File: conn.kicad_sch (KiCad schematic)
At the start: 39 parts, among them J401 PWR IN, J402 Toolhead 1, J403 Toolhead 2, J404 XH, J405 IN, J406 OUT, J407 OUT, Q401 CJAC70P06, U401 TJA1051TK-3, U402 CH334F, U403 USBLC6-2SC6, U404 USBLC6-2SC6, U405 USBLC6-2SC6

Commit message: Major hardware update: toolhead switching, DC/DC protection, and documentation overhaul
Hardware Changes:
- Replaced reverse polarity protection with 2x PFET toolhead switching (PB2/PA5 control)
- Added SS56 Schottky diode reverse polarity protection for DC/DC converter
- Updated current limit resistor to 5.1kΩ (~10.2A)
- Removed fan control circuitry and JST-XH connector
- Removed internal JST-XH USB port with fuse/protection

Documentation Updates:
- Updated both README files to reflect hardware changes
- Removed all fan control references and configurations
- Updated Klipper configuration examples
- Cleaned up pinout and connector assignments
- Updated technical specifications table
- Fixed table of contents and cross-references
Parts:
- removed F405: 1.5A, Fuse:Fuse_0805_2012Metric, symbol Device:Fuse_Small
- removed J404: XH, Connector_JST:JST_XH_B4B-XH-A_1x04_P2.50mm_Vertical, symbol Connector:Conn_01x04_Pin
- removed R402: 30k, Resistor_SMD:R_0402_1005Metric, symbol Device:R
- added D402: D_Schottky, Diode_SMD:D_SMC, symbol Device:D_Schottky
- added D407: BZT52C15S, Diode_SMD:D_SOD-323, symbol Device:D_Zener_Small
- added Q403, Q405: AO3400A, Package_TO_SOT_SMD:SOT-23, symbol Transistor_FET:AO3400A
- added Q404: CJAC70P06, Package_DFN_QFN:AO_DFN-8-1EP_5.55x5.2mm_P1.27mm_EP4.12x4.6mm, symbol Transistor_FET:AON6411
- added R403, R406, R413, R414, R415: 30k, Resistor_SMD:R_0402_1005Metric, symbol Device:R
- added R407, R416: 1k, Resistor_SMD:R_0402_1005Metric, symbol Device:R
- renumbered D402 to D404, D404 to D406, R403 to R405, R404 to R408, R405 to R409, R406 to R410, R407 to R411, R408 to R412
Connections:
- net 24V: now also D402.1 (K); no longer F401.1, F402.1, Q401.5 (D)
- net GND: now also Q403.2 (S), Q405.2 (S), R406.1, R415.1
- net OUT1: now also F401.1, Q404.5 (D); no longer F401.2, J402.1 (Pin_1)
- net OUT2: now also F402.1, Q401.5 (D); no longer F402.2, J403.1 (Pin_1)
- net VEXT: now also D402.2 (A), D407.1 (K), Q404.1 (S), Q404.2 (S), Q404.3 (S), R413.1
- net GATE renamed HE GATE 2
- net HE GATE 2: now also R403.1
- new net: Q405.1 (G), R415.2, R416.1
- new net: Q403.1 (G), R406.2, R407.1
- new net: Q403.3 (D), R403.2
- new net: Q405.3 (D), R414.2
- new net HE GATE 1: D407.2 (A), Q404.4 (G), R413.2, R414.1
- new net HE1 ON: R416.2
- new net HE2 ON: R407.2
- new net OUT1F: F401.2, J402.1 (Pin_1)
- new net OUT2F: F402.2, J403.1 (Pin_1)
- no-connect marks 4 -> 12
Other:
- company: (none) -> Eduard Iten
- title: (none) -> EWS - Power, CANbus and USB HAT for 3D Printers
- moved on the sheet: C401, C402, C403, C404, D403, D404, D405, D406, F401, F402, F404, J402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

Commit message: EWS Rev 0.1 - Complete design with documentation
Release Features:
- Universal HAT for Raspberry Pi 4/5 and Radxa Rock 5B/5B+
- 8A DC/DC converter with SS56 reverse polarity protection
- Dual toolhead switching via PFETs (PB2/PA5 control)
- Native CAN and USB-CAN bridge support
- USB hub with power delivery for touchscreens
- Comprehensive safety features and thermal management

Hardware:
- STM32G0B1KBU6 MCU with crystal-less design
- MaxLinear XR76208 switching regulator
- MCP2542WFD CAN transceiver with jumper selection
- WCH CH334F USB hub with MTT support
- 2oz copper PCB recommended for thermal performance

Documentation:
- Bilingual documentation (German/English)
- Installation guides with kernel diagnostics
- Klipper configuration examples
- Comprehensive problem statement and solutions
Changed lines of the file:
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@@
 	)
 	(junction
-		(at 186.69 78.74)
-		(diameter 0)
-		(color 0 0 0 0)
-	)
-	(junction
 		(at 246.38 45.72)
 		(diameter 0)
@@
 	)
 	(junction
-		(at 186.69 33.02)
-		(diameter 0)
-		(color 0 0 0 0)
-	)
-	(junction
 		(at 88.9 189.23)
 		(diameter 0)
@@
 	)
 	(junction
+		(at 186.69 78.74)
+		(diameter 0)
+		(color 0 0 0 0)
+	)
+	(junction
 		(at 163.83 99.06)
 		(diameter 0)
@@
 	(wire
 		(pts
+			(xy 186.69 76.2) (xy 186.69 78.74)
+		)
+		(stroke
+			(width 0)
+			(type default)
+		)
+	)
+	(wire
+		(pts
 			(xy 60.96 148.59) (xy 60.96 153.67)
 		)
@@
 	(wire
 		(pts
-			(xy 186.69 33.02) (xy 186.69 78.74)
-		)
-		(stroke
-			(width 0)
-			(type default)
-		)
-	)
-	(wire
-		(pts
 			(xy 266.7 157.48) (xy 266.7 158.75)
 		)
@@
 					(unit 1)
 				)
+			)
+		)
+	)
+	(symbol
+		(lib_id "power:+5V")
+		(at 186.69 76.2 0)
+		(unit 1)
+		(exclude_from_sim no)
+		(in_bom yes)
+		(on_board yes)
+		(dnp no)
+		(fields_autoplaced yes)
+		(property "Reference" "#PWR0411"
+			(at 186.69 80.01 0)
+			(effects
+				(font
+					(size 1.27 1.27)
+				)
+				(hide yes)
+			)
+		)
+		(property "Value" "5V"
+			(at 186.69 71.12 0)
+			(effects
+				(font
+					(size 1.27 1.27)
+				)
+			)
+		)
+		(property "Footprint" ""
+			(at 186.69 76.2 0)
+			(effects
+				(font
+					(size 1.27 1.27)
+				)
+				(hide yes)
+			)
+		)
+		(property "Datasheet" ""
+			(at 186.69 76.2 0)
+			(effects
+				(font
+					(size 1.27 1.27)
+				)
+				(hide yes)
+			)
+		)
+		(property "Description" "Power symbol creates a global label with name \"+5V\""
+			(at 186.69 76.2 0)
+			(effects
+				(font
+					(size 1.27 1.27)
+				)
+				(hide yes)
+			)
+		)
+		(pin "1"
+		)
+		(instances
+			(project "EWS"
+				(path "/4ae99543-64c8-472f-befd-04c32f138656/7e492d82-58e4-4d5e-a79a-918a5cf15050"
+					(reference "#PWR0411")
+					(unit 1)
+				)

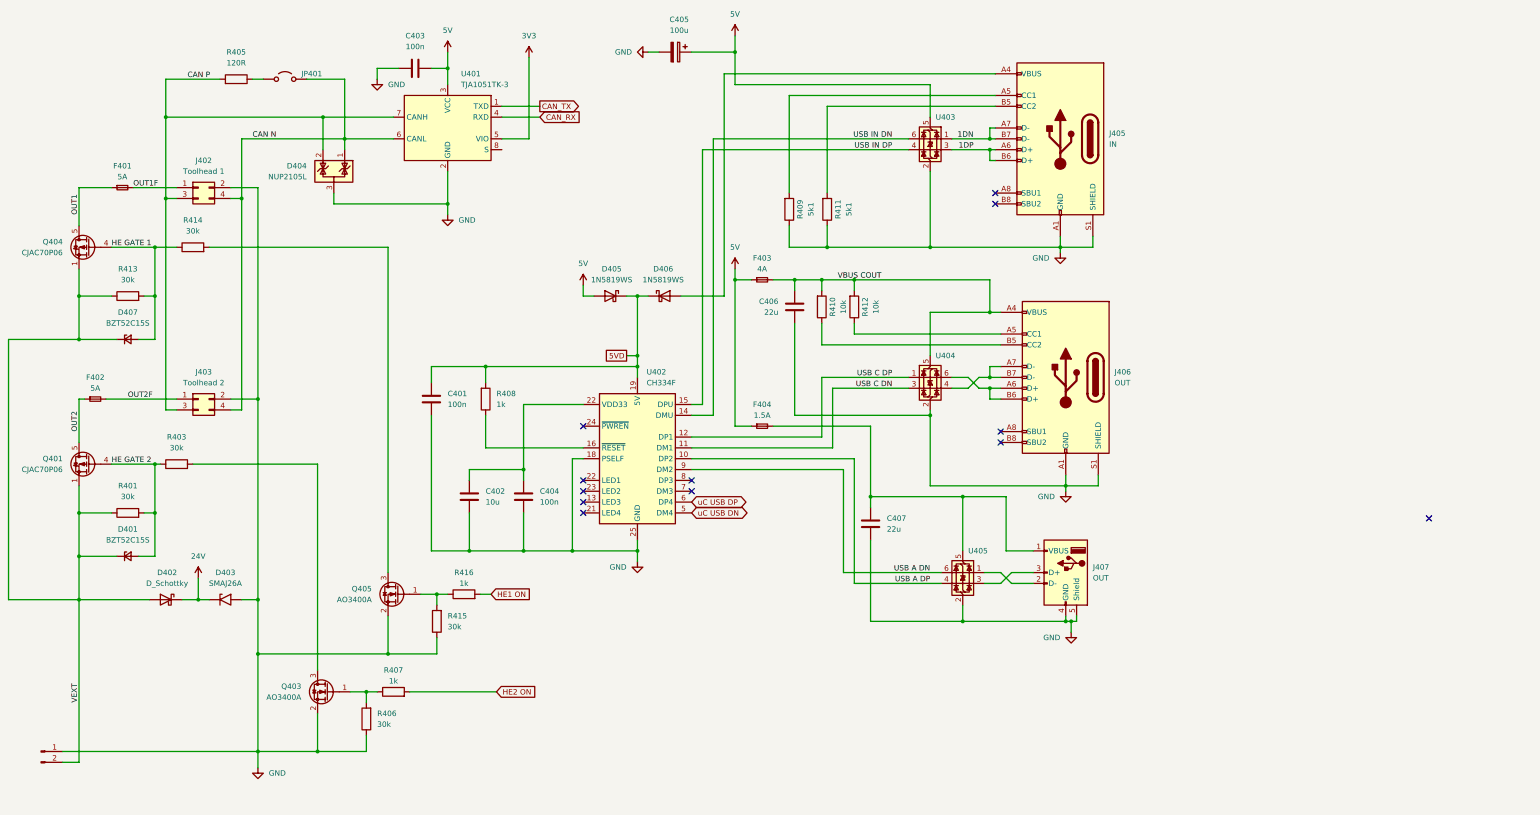
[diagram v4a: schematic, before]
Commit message: Schema improvements and CAN transceiver modification
- Improved schema layout for better readability and organization
- Connected CAN transceiver S-pin to GND for proper operation
- Updated PCB layout to reflect schema changes
- Enhanced component placement and routing clarity
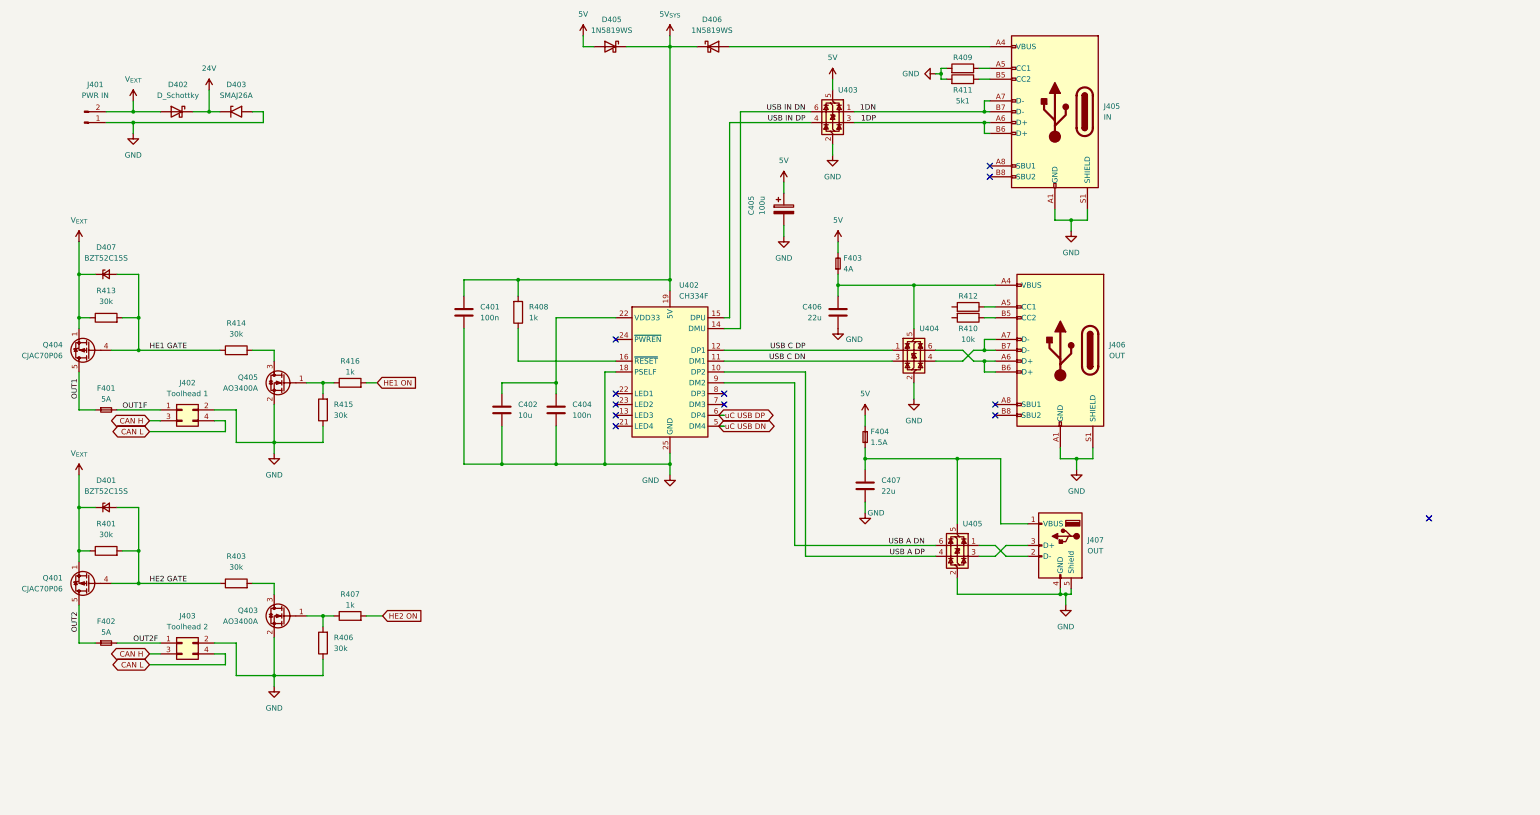
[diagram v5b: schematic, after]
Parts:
- removed C403: 100n, Capacitor_SMD:C_0402_1005Metric, symbol Device:C
- removed D404: NUP2105L, Package_TO_SOT_SMD:SOT-23, symbol Power_Protection:NUP2105L
- removed JP401: ~, Connector_PinHeader_2.54mm:PinHeader_1x02_P2.54mm_Vertical, symbol Jumper:Jumper_2_Open
- removed R405: 120R, Resistor_SMD:R_0402_1005Metric_Pad0.72x0.64mm_HandSolder, symbol Device:R
- removed U401: TJA1051TK-3, Package_SON:HVSON-8-1EP_3x3mm_P0.65mm_EP1.6x2.4mm, symbol Interface_CAN_LIN:TJA1051TK-3
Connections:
- net 5V: now also F403.2; no longer F403.1
- net GND: now also R409.2, R411.2; no longer R409.1, R411.1
- net at J405.B5 (CC2): now also R411.1; no longer R411.2
- net at J405.A5 (CC1): now also R409.1; no longer R409.2
- net 5VD renamed 5V_{SYS}
- net CAN N renamed CAN L
- net CAN P renamed CAN H
- net HE GATE 1 renamed HE1 GATE
- net HE GATE 2 renamed HE2 GATE
- net VBUS COUT: no longer names the net of C406.1, J406.A4 (VBUS), J406.A9 (VBUS), J406.B4 (VBUS), J406.B9 (VBUS), U404.5 (VBUS)
- net VBUS COUT: now also F403.1; no longer F403.2, R410.2, R412.2
- net VEXT renamed V_{EXT}
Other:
- moved on the sheet: C401, C402, C404, C405, C406, C407, D401, D402, D403, D405, D406, D407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

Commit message: Rev 0.2: Major hardware improvements and production readiness
Hardware Improvements (Thanks to shx for schematic cleanup):
- Clean up schematic organization and structure
- Set CAN transceiver Silent pin to GND for stability
- Add status LEDs (yellow: 24V/5V/3.3V, green: MCU PB4)
- Replace jumpers with solder jumpers on bottom side
- Add jumpers to output PFETs for permanent-on without firmware
- Add robust test points for 5V/GND load testing
- Add optional heatsink for DC/DC converter on bottom
- Add 10µF capacitor for MCU on 3.3V rail

Component Optimizations:
- Replace 30kΩ with 33kΩ basic part for simplified BOM
- Change DC/DC feedback: 15.5kΩ15kΩ (new output: 5.1V)
- Upgrade CAN ESD protection: NUP2105LPESD1CAN
- Increase CAN termination resistor footprint: 04020603
- Switch USB hub supply from 5V to 3.3V per datasheet

Production Ready:
- Add all LCSC part numbers and rotations
- Generate complete production data package
- Improve PCB layout and button placement
- Create comprehensive changelog documentation
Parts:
- removed R416: 1k, Resistor_SMD:R_0402_1005Metric, symbol Device:R
- added JP401, JP402: ~, project:SolderJumper-3_P1.3mm_Bridged12_RoundedPad1.0x1.5mm_custom, symbol Jumper:Jumper_3_Bridged12
- C401, C404: LCSC Part # (none) -> C307331; Manufacturer Part # (none) -> CL05B104KB54PNC
- C402: LCSC Part # (none) -> C96446; Manufacturer Part # (none) -> CL10A106MA8NRNC
- C405: renamed from C406; LCSC Part # (none) -> C12891; Manufacturer Part # (none) -> CL31A226KAHNNNE
- C406: renamed from C407; LCSC Part # (none) -> C12891; Manufacturer Part # (none) -> CL31A226KAHNNNE
- D403: renamed from D402; value D_Schottky -> SS56; LCSC Part # (none) -> C24138; Manufacturer Part # (none) -> SS56C
- D404: renamed from D403; LCSC Part # (none) -> C19077543; Manufacturer Part # (none) -> SMAJ26A
- D405, D406: LCSC Part # (none) -> C191023; Manufacturer Part # (none) -> 1N5819WS
- F401, F402: LCSC Part # (none) -> C163128; Manufacturer Part # (none) -> CFS12V3T5R0
- F403: LCSC Part # C49305071 -> C2680546; Manufacturer Part # BSMD0805L-400 -> JK-SMD-0805-400L-12
- J401: value PWR IN -> XT30; FT Rotation Offset (none) -> 180; LCSC Part # (none) -> C431092; Manufacturer Part # (none) -> XT30PW-M30.G.Y
- J402: value Toolhead 1 -> MX3.0 2x2; FT Rotation Offset (none) -> 180; LCSC Part # (none) -> C122413; Manufacturer Part # (none) -> 430450400
- J403: value Toolhead 2 -> MX3.0 2x2; FT Rotation Offset (none) -> 180; LCSC Part # (none) -> C122413; Manufacturer Part # (none) -> 430450400
- J404: renamed from J405; value IN -> USB-C
- J405: renamed from J406; value OUT -> USB-C
- J406: renamed from J407; value OUT -> USB-A
- Q401: renamed from Q404; FT Rotation Offset (none) -> 270; LCSC Part # (none) -> C2898279; Manufacturer Part # (none) -> CJAC70P06
- Q402: renamed from Q401; FT Rotation Offset (none) -> 270; LCSC Part # (none) -> C2898279; Manufacturer Part # (none) -> CJAC70P06
- Q403: renamed from Q405; LCSC Part # (none) -> C20917; Manufacturer Part # (none) -> AO3400A
- Q404: renamed from Q403; LCSC Part # (none) -> C20917; Manufacturer Part # (none) -> AO3400A
- R401: renamed from R413; value 30k -> 33k; LCSC Part # (none) -> C25779; Manufacturer Part # (none) -> 0402WGF3302TCE
- R402: renamed from R401; value 30k -> 33k; LCSC Part # (none) -> C25779; Manufacturer Part # (none) -> 0402WGF3302TCE
- R403: renamed from R414; value 30k -> 33k; LCSC Part # (none) -> C25779; Manufacturer Part # (none) -> 0402WGF3302TCE
- R404: renamed from R403; value 30k -> 33k; LCSC Part # (none) -> C25779; Manufacturer Part # (none) -> 0402WGF3302TCE
- R405: renamed from R415; value 30k -> 33k; LCSC Part # (none) -> C25779; Manufacturer Part # (none) -> 0402WGF3302TCE
- R406: value 30k -> 33k; LCSC Part # (none) -> C25779; Manufacturer Part # (none) -> 0402WGF3302TCE
- R407, R408: LCSC Part # (none) -> C11702; Manufacturer Part # (none) -> 0402WGF1001TCE
- R409: LCSC Part # (none) -> C25905; Manufacturer Part # (none) -> 0402WGF5101TCE
- R410: renamed from R411; LCSC Part # (none) -> C25905; Manufacturer Part # (none) -> 0402WGF5101TCE
- R411: renamed from R412; LCSC Part # (none) -> C25744; Manufacturer Part # (none) -> 0402WGF1002TCE
- R412: renamed from R410; LCSC Part # (none) -> C25744; Manufacturer Part # (none) -> 0402WGF1002TCE
- U401: renamed from U402; LCSC Part # (none) -> C5187527; Manufacturer Part # (none) -> CH334F
- U402: renamed from U403; FT Rotation Offset (none) -> 90; LCSC Part # (none) -> C2687116; Manufacturer Part # (none) -> USBLC6-2SC6
- U403: renamed from U404; FT Rotation Offset (none) -> 90; LCSC Part # (none) -> C2687116; Manufacturer Part # (none) -> USBLC6-2SC6
- U404: renamed from U405; FT Rotation Offset (none) -> 90; LCSC Part # (none) -> C2687116; Manufacturer Part # (none) -> USBLC6-2SC6
- renumbered C405 to C403, D407 to D401, D401 to D402
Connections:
- net 5V: now also F403.1; no longer F403.2
- net 5V_{SYS}: no longer C401.1, R408.2, U401.19 (5V)
- net GND: no longer U401.18 (PSELF)
- net HE1 ON: now also R407.1
- net HE2 ON: now also R408.1; no longer R407.2
- net USB A DN: now also U401.10 (DP2), U404.1 (I/O1); no longer U401.9 (DM2), U404.6 (I/O1)
- net USB A DP: now also U401.9 (DM2), U404.3 (I/O2); no longer U401.10 (DP2), U404.4 (I/O2)
- net at Q403.1 (G), R405.2: now also JP401.2 (C)
- net at Q404.1 (G), R406.2: now also JP402.2 (C); no longer R407.1
- net at U401.16 (~{RESET}): no longer R408.1
- net at R412.2: now also C405.1, F403.2, J405.A4 (VBUS), J405.A9 (VBUS), J405.B4 (VBUS), J405.B9 (VBUS), R411.2, U403.5 (VBUS)
- net 3V3: now reaches C402.1, C404.1
- net 3V3: now also C401.1, U401.1 (~{OVCUR}), U401.19 (5V), U401.20 (VDD33), JP401.3 (B), JP402.3 (B); no longer U401.22 (LED1)
- net at J406.2 (D-): now also U404.4 (I/O2); no longer U404.1 (I/O1)
- net at J406.3 (D+): now also U404.6 (I/O1); no longer U404.3 (I/O2)
- new net: JP401.1 (A), R407.2
- new net: JP402.1 (A), R408.2
- no-connect marks 12 -> 8
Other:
- moved on the sheet: C401, C403
